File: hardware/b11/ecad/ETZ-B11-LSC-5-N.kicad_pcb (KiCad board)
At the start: 2 copper layers, 112.3 x 85.8 mm, 0 parts

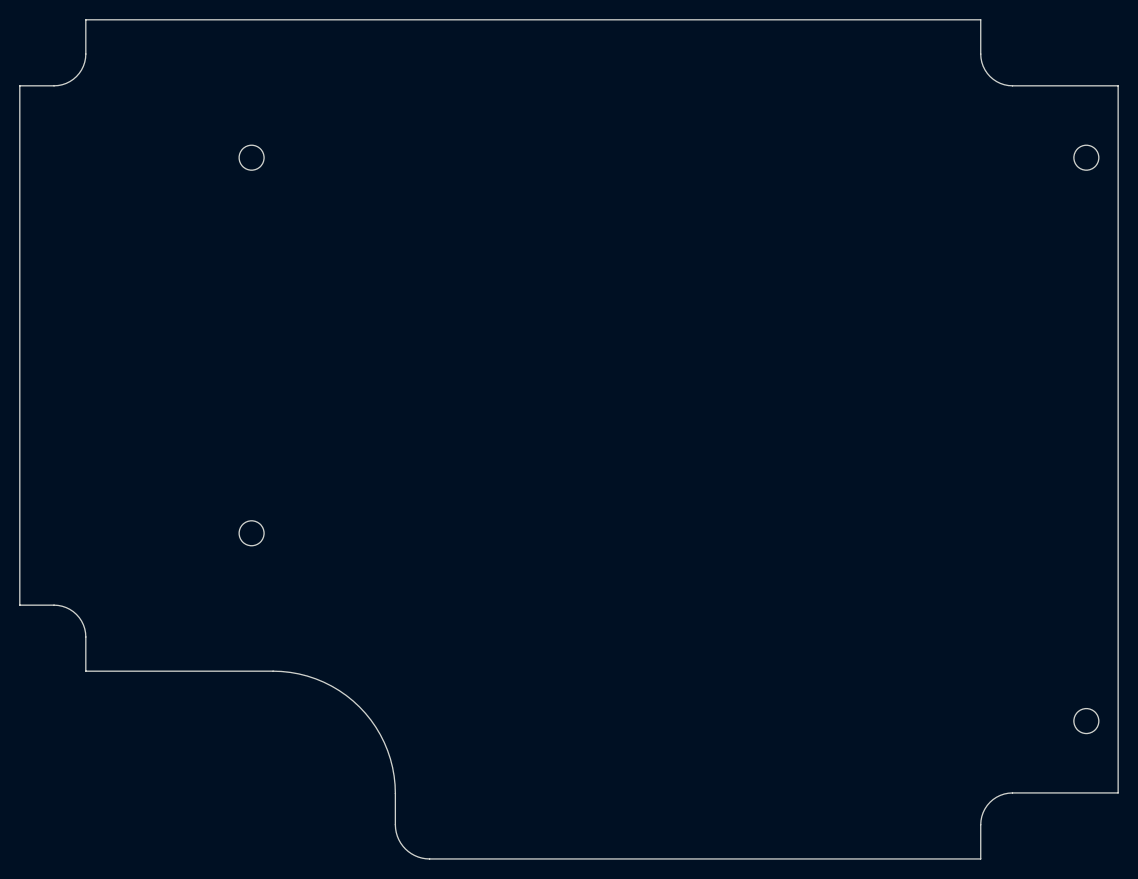
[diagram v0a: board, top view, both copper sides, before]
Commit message: feat(hardware/b11): place MX hotswap switches on normal-profile carrier PCBs
Add place-b11-switches.py with SWIG pre-init workaround (plug must be
created and FootprintLoad called before LoadBoard or SWIG type registry
gets corrupted). Layout: 5-col boards get 18 switches (15 main + 3
thumb at cols 2-4), 6-col get 22 (18 main + 4 thumb at cols 2-5).

Also refresh all 20 PCB outline DXFs from latest MCAD release and add
MX_V2 footprint library as a submodule.

Co-Authored-By: Claude Sonnet 4.6 <noreply@anthropic.com>
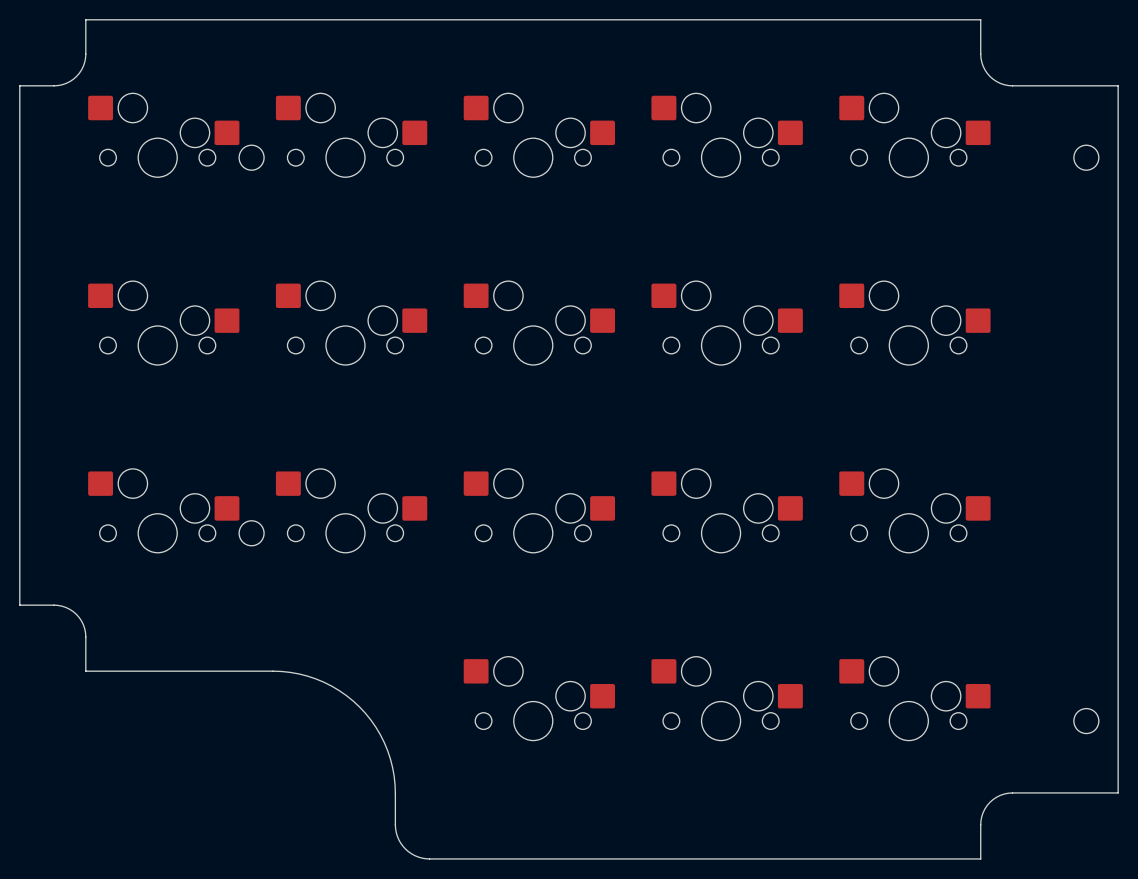
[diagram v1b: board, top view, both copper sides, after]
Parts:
- added SW1: MX-Hotswap-1U, MX-Hotswap-1U, F.Cu at (106.4, 73.3)
- added SW10: MX-Hotswap-1U, MX-Hotswap-1U, F.Cu at (183.2, 92.5)
- added SW11: MX-Hotswap-1U, MX-Hotswap-1U, F.Cu at (106.4, 111.7)
- added SW12: MX-Hotswap-1U, MX-Hotswap-1U, F.Cu at (125.6, 111.7)
- added SW13: MX-Hotswap-1U, MX-Hotswap-1U, F.Cu at (144.8, 111.7)
- added SW14: MX-Hotswap-1U, MX-Hotswap-1U, F.Cu at (164.0, 111.7)
- added SW15: MX-Hotswap-1U, MX-Hotswap-1U, F.Cu at (183.2, 111.7)
- added SW16: MX-Hotswap-1U, MX-Hotswap-1U, F.Cu at (144.8, 130.9)
- added SW17: MX-Hotswap-1U, MX-Hotswap-1U, F.Cu at (164.0, 130.9)
- added SW18: MX-Hotswap-1U, MX-Hotswap-1U, F.Cu at (183.2, 130.9)
- added SW2: MX-Hotswap-1U, MX-Hotswap-1U, F.Cu at (125.6, 73.3)
- added SW3: MX-Hotswap-1U, MX-Hotswap-1U, F.Cu at (144.8, 73.3)
- added SW4: MX-Hotswap-1U, MX-Hotswap-1U, F.Cu at (164.0, 73.3)
- added SW5: MX-Hotswap-1U, MX-Hotswap-1U, F.Cu at (183.2, 73.3)
- added SW6: MX-Hotswap-1U, MX-Hotswap-1U, F.Cu at (106.4, 92.5)
- added SW7: MX-Hotswap-1U, MX-Hotswap-1U, F.Cu at (125.6, 92.5)
- added SW8: MX-Hotswap-1U, MX-Hotswap-1U, F.Cu at (144.8, 92.5)
- added SW9: MX-Hotswap-1U, MX-Hotswap-1U, F.Cu at (164.0, 92.5)

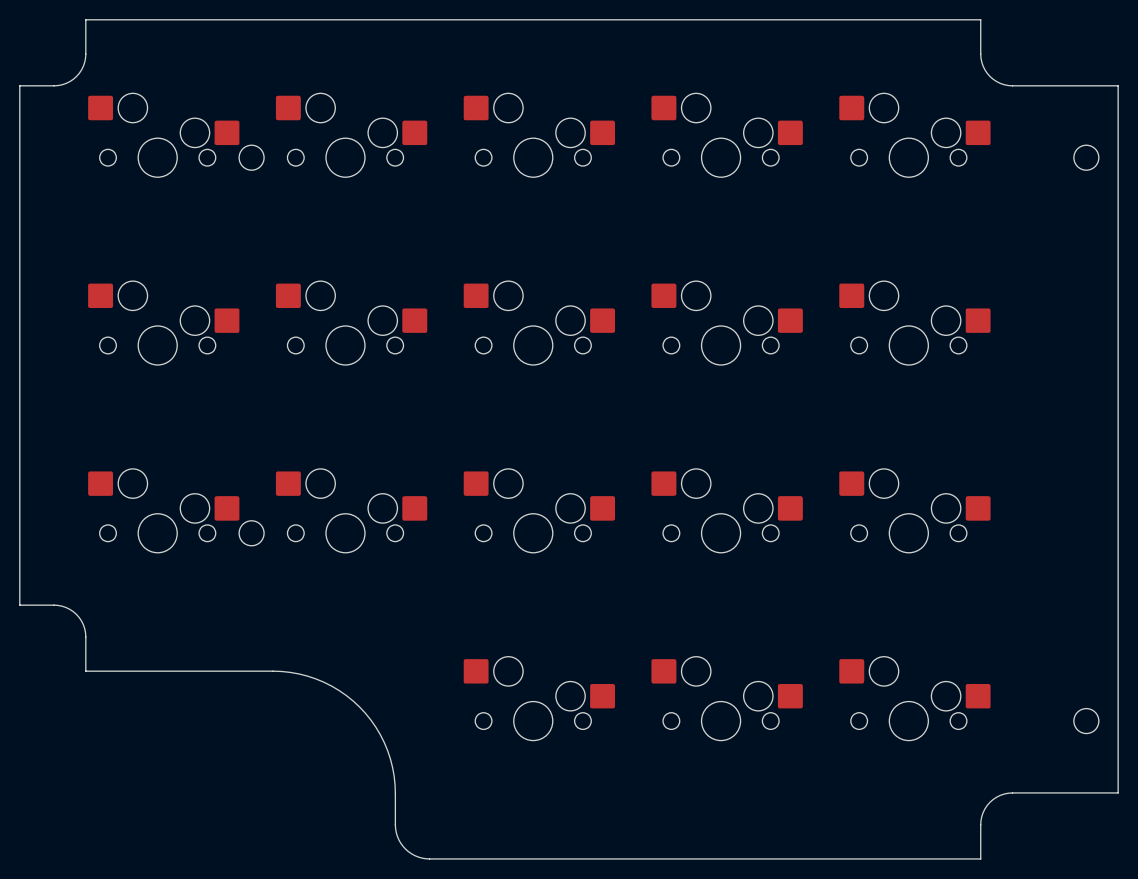
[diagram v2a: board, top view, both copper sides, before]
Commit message: feat(hardware/b11): place hotswap sockets on all carrier boards, south-facing
- Place Kailh MX hotswap sockets (MX-Hotswap-1U) on 4 normal-profile carrier
  boards at 19.2mm pitch, flipped to B.Cu, 180° south-facing orientation
- Place Kailh Choc v1 hotswap sockets (PG1350) on 4 low-profile carrier boards
  at 19.2mm pitch, 180° south-facing orientation
- Add 3D model (Kailh-Choc-Socket-CPG135001S30.step) to PG1350 footprint with
  correct offset/rotation for B.Cu-pad, F.Cu-module placement
- Strip F.SilkS, F.Fab, F.CrtYd top-layer graphics from LP carrier PG1350 footprints
- Rename place-b11-switches.py → place-b11-switches-np.py for symmetry with new lp script
- Add place-b11-switches-lp.py for Choc v1 placement automation

Co-Authored-By: Claude Sonnet 4.6 <noreply@anthropic.com>
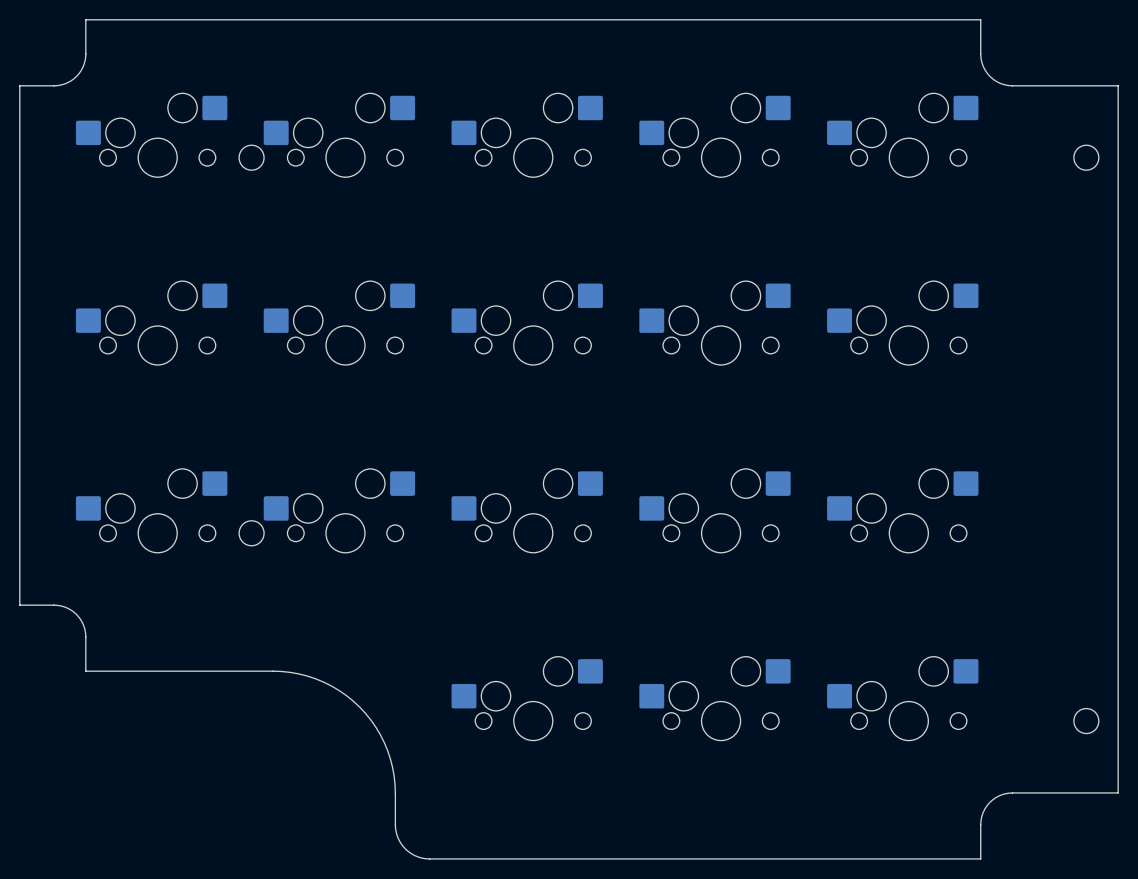
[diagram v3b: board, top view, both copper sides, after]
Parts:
- SW1, SW10, SW11, SW12, SW13, SW14, SW15, SW16, SW17, SW18, SW2, SW3, SW4, SW5, SW6, SW7, SW8, SW9: moved to B.Cu
- turned SW1 to 180 degrees
- turned SW10 to 180 degrees
- turned SW11 to 180 degrees
- turned SW12 to 180 degrees
- turned SW13 to 180 degrees
- turned SW14 to 180 degrees
- turned SW15 to 180 degrees
- turned SW16 to 180 degrees
- turned SW17 to 180 degrees
- turned SW18 to 180 degrees
- turned SW2 to 180 degrees
- turned SW3 to 180 degrees
- turned SW4 to 180 degrees
- turned SW5 to 180 degrees
- turned SW6 to 180 degrees
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
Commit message: feat(hardware/b11): add SMD 6028 back-mount LED footprint and place on all carrier PCBs
- Add LED_SMD_6028_BackMount footprint with router-safe rounded-rectangle
  slot cutout (3.3 × 3.9 mm, 0.5 mm corners, 1 mm bit), roundrect pads
  (1.4 × 2.8 mm, 25% ratio), silkscreen polarity markers clear of pads
- Add LED_SMD_6028.step 3D model from 3D Content Central
- Add place-b11-leds.py: places 18–22 LEDs per carrier PCB aligned to
  the switch grid, 5.9 mm south of each switch center
- Place LEDs on all 8 carrier PCBs (LSC/RSC × 5/6-col × N/L)

Co-Authored-By: Claude Sonnet 4.6 <noreply@anthropic.com>
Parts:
- added LED1: LED_SMD_6028_BackMount, LED_SMD_6028_BackMount, B.Cu at (106.4, 79.2)
- added LED10: LED_SMD_6028_BackMount, LED_SMD_6028_BackMount, B.Cu at (183.2, 98.4)
- added LED11: LED_SMD_6028_BackMount, LED_SMD_6028_BackMount, B.Cu at (106.4, 117.6)
- added LED12: LED_SMD_6028_BackMount, LED_SMD_6028_BackMount, B.Cu at (125.6, 117.6)
- added LED13: LED_SMD_6028_BackMount, LED_SMD_6028_BackMount, B.Cu at (144.8, 117.6)
- added LED14: LED_SMD_6028_BackMount, LED_SMD_6028_BackMount, B.Cu at (164.0, 117.6)
- added LED15: LED_SMD_6028_BackMount, LED_SMD_6028_BackMount, B.Cu at (183.2, 117.6)
- added LED16: LED_SMD_6028_BackMount, LED_SMD_6028_BackMount, B.Cu at (144.8, 136.8)
- added LED17: LED_SMD_6028_BackMount, LED_SMD_6028_BackMount, B.Cu at (164.0, 136.8)
- added LED18: LED_SMD_6028_BackMount, LED_SMD_6028_BackMount, B.Cu at (183.2, 136.8)
- added LED2: LED_SMD_6028_BackMount, LED_SMD_6028_BackMount, B.Cu at (125.6, 79.2)
- added LED3: LED_SMD_6028_BackMount, LED_SMD_6028_BackMount, B.Cu at (144.8, 79.2)
- added LED4: LED_SMD_6028_BackMount, LED_SMD_6028_BackMount, B.Cu at (164.0, 79.2)
- added LED5: LED_SMD_6028_BackMount, LED_SMD_6028_BackMount, B.Cu at (183.2, 79.2)
- added LED6: LED_SMD_6028_BackMount, LED_SMD_6028_BackMount, B.Cu at (106.4, 98.4)
- added LED7: LED_SMD_6028_BackMount, LED_SMD_6028_BackMount, B.Cu at (125.6, 98.4)
- added LED8: LED_SMD_6028_BackMount, LED_SMD_6028_BackMount, B.Cu at (144.8, 98.4)
- added LED9: LED_SMD_6028_BackMount, LED_SMD_6028_BackMount, B.Cu at (164.0, 98.4)

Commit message: fix(hardware/b11): fix switch socket placement, 3D models, and submodule pins
- Pin MX_V2 submodule to ab59b57 (before upstream "topside pads" change that
  moved SMD pads to F.Cu — old commit has correct B.Cu pads natively)
- Fix SWIG type-registry corruption in both switch placement scripts by
  pre-loading all footprint instances and caching pad refs before LoadBoard()
- Fix LP script: add make_patched_lib to rewrite Choc socket 3D model path
  to absolute path and convert old (at ...) inch offset to (offset ...) mm
  format — KiCad 9 was multiplying the old format by 25.4, placing model
  127mm off-center
- Regenerate all 8 carrier PCBs with updated board outlines (LSC-6 mounting
  hole positions) and correctly placed switches + LEDs

Co-Authored-By: Claude Sonnet 4.6 <noreply@anthropic.com>
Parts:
- SW1, SW10, SW11, SW12, SW13, SW14, SW15, SW16, SW17, SW18, SW2, SW3, SW4, SW5, SW6, SW7, SW8, SW9: moved to F.Cu
- turned SW1 to 0 degrees
- turned SW10 to 0 degrees
- turned SW11 to 0 degrees
- turned SW12 to 0 degrees
- turned SW13 to 0 degrees
- turned SW14 to 0 degrees
- turned SW15 to 0 degrees
- turned SW16 to 0 degrees
- turned SW17 to 0 degrees
- turned SW18 to 0 degrees
- turned SW2 to 0 degrees
- turned SW3 to 0 degrees
- turned SW4 to 0 degrees
- turned SW5 to 0 degrees
- turned SW6 to 0 degrees
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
